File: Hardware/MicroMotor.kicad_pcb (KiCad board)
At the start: 4 copper layers, 108.4 x 72.2 mm, 109 parts, among them J1 USB_C_Receptacle_USB2.0, J2 Conn_01x04_Male, J3 Conn_01x05_Male, Q1 FDB075N15A, Q2 FDB075N15A, Q3 FDB075N15A, Q4 FDB075N15A, Q5 FDB075N15A, Q6 FDB075N15A, SW1 SW_Push, U1 FT230XQ-T, U10 LP2985-3.3, U11 NC7WZ04, U2 STM32F410RBTx, U3 ACSL-6210-00RE, U4 LM2594HVM-12, U5 INA240A3D, U6 INA240A3D, U7 LP2985-5.0, U9 HIP4086ABZ

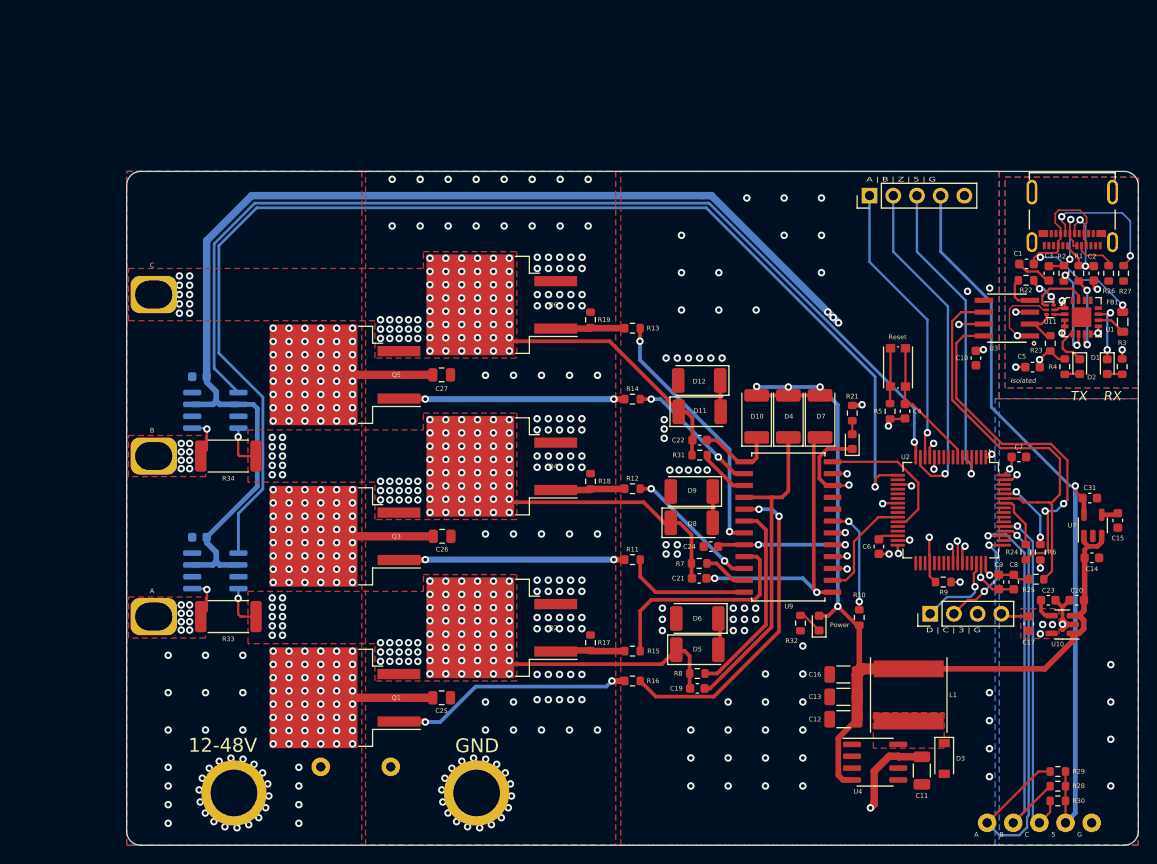
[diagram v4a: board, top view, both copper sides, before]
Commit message: Made board into pluggable two-board solution.
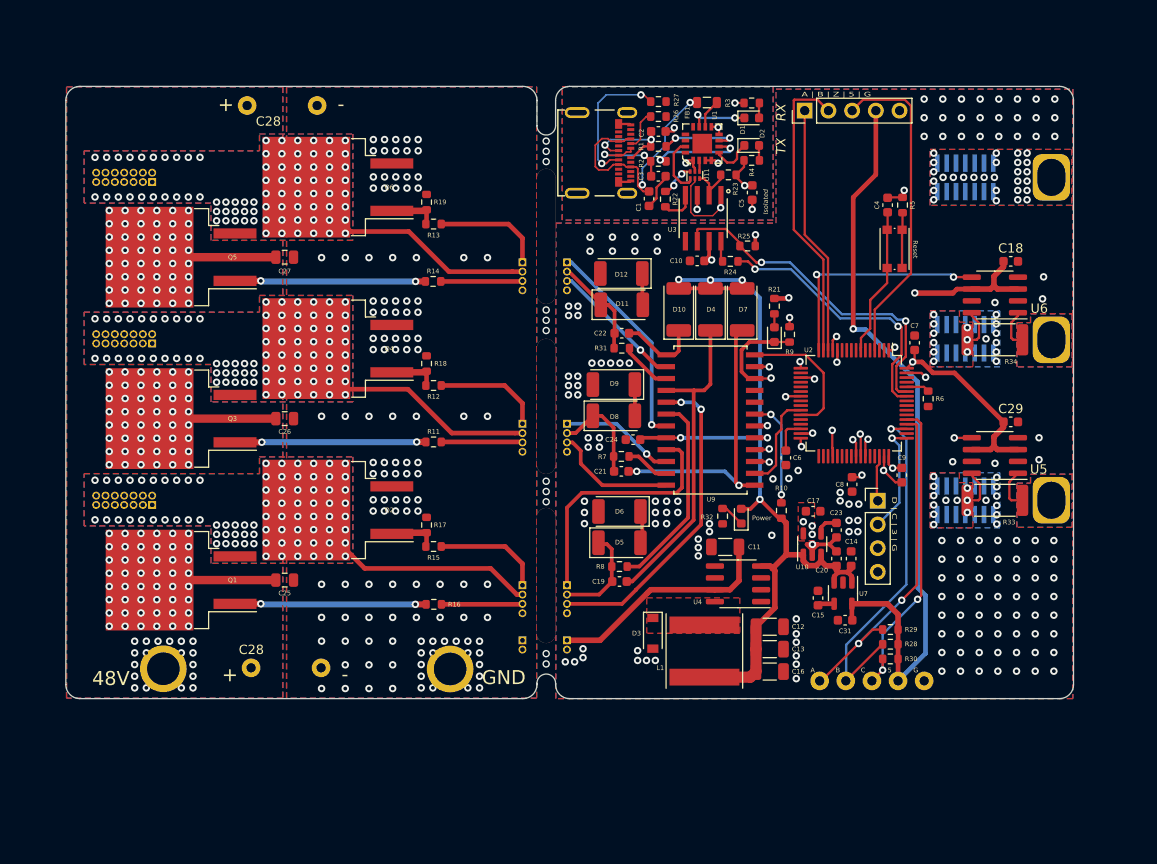
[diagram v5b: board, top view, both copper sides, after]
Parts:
- removed 12-48V: TestPoint_THTPad_D4.0mm_Drill2.0mm, TestPoint:TestPoint_THTPad_D4.0mm_Drill2.0mm
- removed the C28 at (124.0, 135.6)
- added 48V: TestPoint_THTPad_D4.0mm_Drill2.0mm, TestPoint:TestPoint_THTPad_D4.0mm_Drill2.0mm, F.Cu at (102.7, 126.1)
- added C28: 1000uF, Capacitor_THT:C_Radial_D18.0mm_H35.5mm_P7.50mm, F.Cu at (116.1, 64.7)
- added C28: 1000uF, Capacitor_THT:C_Radial_D18.0mm_H35.5mm_P7.50mm, F.Cu at (116.5, 125.0)
- added J10: Conn_02x06_Odd_Even, Connector_PinSocket_1.00mm:PinSocket_2x07_P1.00mm_Vertical_SMD, B.Cu at (193.1, 72.4)
- added J11: Conn_02x06_Odd_Even, Connector_PinSocket_1.00mm:PinSocket_2x07_P1.00mm_Vertical_SMD, B.Cu at (193.1, 89.7)
- added J12: Conn_02x06_Odd_Even, Connector_PinSocket_1.00mm:PinSocket_2x07_P1.00mm_Vertical_SMD, B.Cu at (193.1, 107.0)
- added J13: Conn_01x04_Female, Connector_PinSocket_1.00mm:PinSocket_1x04_P1.00mm_Vertical, B.Cu at (150.4, 81.5)
- added J14: Conn_01x04_Female, Connector_PinSocket_1.00mm:PinSocket_1x04_P1.00mm_Vertical, B.Cu at (150.4, 98.8)
- added J15: Conn_01x04_Female, Connector_PinSocket_1.00mm:PinSocket_1x04_P1.00mm_Vertical, B.Cu at (150.4, 116.1)
- added J16: Conn_01x02_Male, Connector_PinHeader_1.00mm:PinHeader_1x02_P1.00mm_Vertical, B.Cu at (145.6, 122.0)
- added J17: Conn_01x02_Female, Connector_PinSocket_1.00mm:PinSocket_1x02_P1.00mm_Vertical, B.Cu at (150.4, 122.0)
- added J4: Conn_01x04_Male, Connector_PinHeader_1.00mm:PinHeader_1x04_P1.00mm_Vertical, B.Cu at (145.6, 81.5)
- added J5: Conn_01x04_Male, Connector_PinHeader_1.00mm:PinHeader_1x04_P1.00mm_Vertical, B.Cu at (145.6, 98.8)
- added J6: Conn_01x04_Male, Connector_PinHeader_1.00mm:PinHeader_1x04_P1.00mm_Vertical, B.Cu at (145.6, 116.1)
- added J7: Conn_02x06_Odd_Even, Connector_PinHeader_1.00mm:PinHeader_2x07_P1.00mm_Vertical, B.Cu at (105.9, 72.9)
- added J8: Conn_02x06_Odd_Even, Connector_PinHeader_1.00mm:PinHeader_2x07_P1.00mm_Vertical, B.Cu at (105.9, 90.2)
- added J9: Conn_02x06_Odd_Even, Connector_PinHeader_1.00mm:PinHeader_2x07_P1.00mm_Vertical, B.Cu at (105.9, 107.5)
- added REF**: Test-Point-Pin_Drill2.79mm, digikey-footprints:Test-Point-Pin_Drill2.79mm, F.Cu at (148.2, 115.1)
- added REF**: Test-Point-Pin_Drill2.79mm, digikey-footprints:Test-Point-Pin_Drill2.79mm, F.Cu at (148.2, 97.0)
- added REF**: Test-Point-Pin_Drill2.79mm, digikey-footprints:Test-Point-Pin_Drill2.79mm, F.Cu at (148.2, 78.8)
- A, B, C: moved to B.Cu
- C18, C29, U5, U6: moved to F.Cu
- moved C 97.6 mm to (202.7, 72.3), turned to 270 degrees
- moved A 97.6 mm to (202.7, 106.9), turned to 270 degrees
- moved B 97.6 mm to (202.7, 89.7), turned to 270 degrees
- moved C18 87.8 mm to (197.9, 81.4), turned to 180 degrees
- moved C29 87.8 mm to (197.9, 98.6), turned to 180 degrees
- moved U5 84.4 mm to (196.2, 102.2), turned to 180 degrees
- moved U6 84.4 mm to (196.2, 85.0), turned to 180 degrees
- moved R33 83.1 mm to (196.2, 107.0), turned to 180 degrees
- moved R34 83.1 mm to (196.2, 89.8), turned to 180 degrees
- moved R27 53.1 mm to (160.2, 64.3), turned to 0 degrees
- moved J1 51.4 mm to (153.5, 69.8), turned to 270 degrees
- moved R26 51.1 mm to (160.2, 65.9), turned to 0 degrees
- moved FB1 50.4 mm to (165.4, 64.4), turned to 180 degrees
- moved C2 49.1 mm to (160.2, 67.5), turned to 0 degrees
- moved R3 48.7 mm to (170.2, 64.5), turned to 0 degrees
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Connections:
- net Net-(R11-Pad1) renamed BHO_r
- net Net-(R12-Pad1) renamed BLO_r
- net Net-(R13-Pad1) renamed CLO_r
- net Net-(R14-Pad1) renamed CHO_r
- net Net-(R15-Pad1) renamed ALO_r
- net Net-(R16-Pad1) renamed AHO_r
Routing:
- net A_SENS: track 130.7 -> 22.5 mm, vias 1 -> 2
- net +3V3: track 143.5 -> 53.0 mm, vias 16 -> 15
- net B_SENS: track 108.2 -> 25.0 mm, vias 1 -> 2
- net Net-(R24-Pad1): track 38.1 -> 2.23 mm, vias 2 -> 0
- net USART1_TX: track 5.90 -> 29.5 mm, vias 0 -> 2
- net 12V_Out: track 117.8 -> 97.1 mm
- net +48V: track 113.6 -> 97.7 mm, vias 180 -> 162
- net ALO_r: track 23.4 -> 38.9 mm
- net HALL_A: track 47.7 -> 36.1 mm, vias 1 -> 2
- net BLO_r: track 14.5 -> 24.0 mm, vias 2 -> 1
- net CHO_r: track 14.4 -> 23.2 mm, vias 2 -> 1
- net USART1_RX: track 45.4 -> 36.8 mm, vias 0 -> 2
- net BHO_r: track 13.7 -> 22.1 mm
- net AHO_r: track 34.9 -> 43.0 mm
- net CLO_r: track 27.4 -> 35.0 mm, vias 2 -> 1
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- added copper zone on B.Cu, net +48V
- added copper zone on B.Cu, net A_OUT
- added copper zone on B.Cu, net B_OUT
- added copper zone on B.Cu, net MTR_A
- added copper zone on B.Cu, net MTR_B
- added copper zone on B.Cu, net MTR_C
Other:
- board size 108.4 x 72.2 mm -> 108 x 65.6 mm
- board text added: "+"
- board text added: "-"

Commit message: More board finalization. More low ESR caps on power stage. Silkscreen fixes.
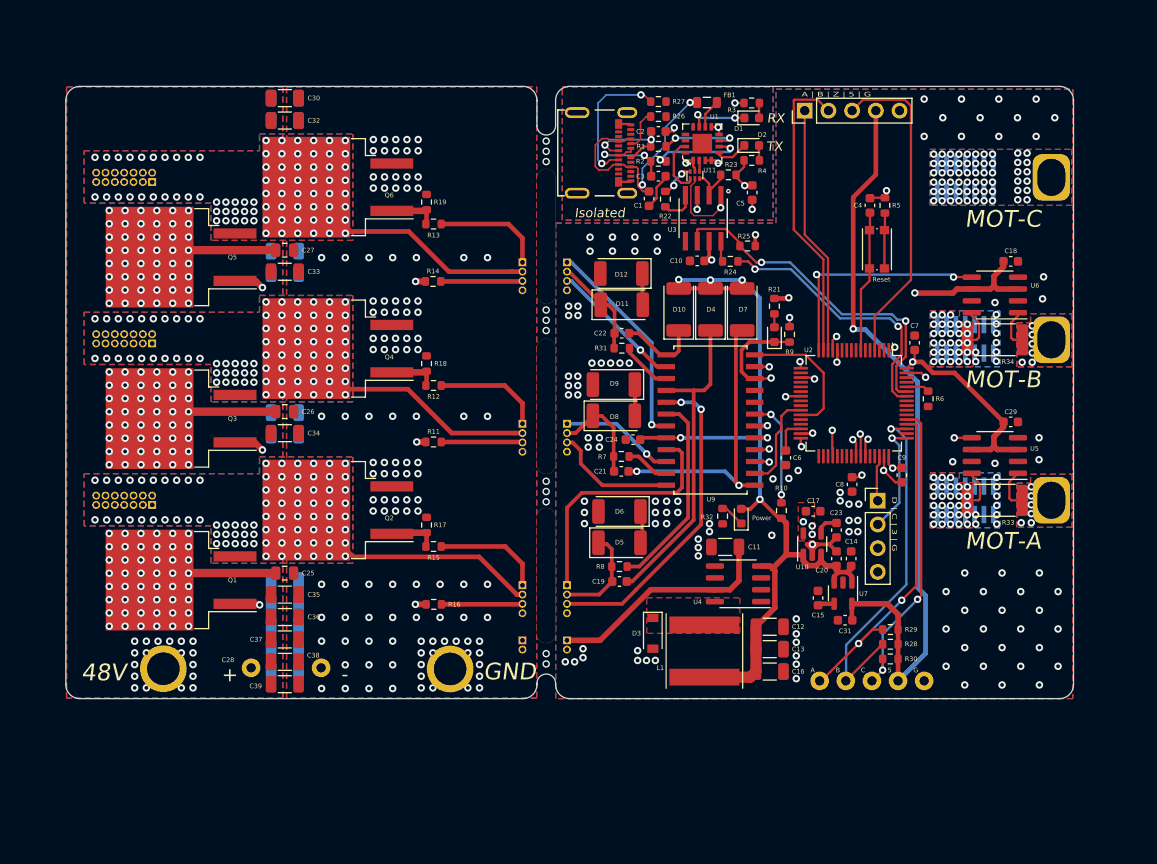
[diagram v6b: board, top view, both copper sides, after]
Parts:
- removed the C28 at (116.1, 64.7)
- added C30: 4.7uF, Capacitor_SMD:C_1206_3216Metric, F.Cu at (120.2, 64.0)
- added C32: 4.7uF, Capacitor_SMD:C_1206_3216Metric, F.Cu at (120.2, 66.3)
- added C33: 4.7uF, Capacitor_SMD:C_1206_3216Metric, F.Cu at (120.2, 82.5)
- added C34: 4.7uF, Capacitor_SMD:C_1206_3216Metric, F.Cu at (120.2, 99.8)
- added C35: 4.7uF, Capacitor_SMD:C_1206_3216Metric, F.Cu at (120.2, 117.2)
- added C36: 4.7uF, Capacitor_SMD:C_1206_3216Metric, F.Cu at (120.2, 119.5)
- added C37: 4.7uF, Capacitor_SMD:C_1206_3216Metric, F.Cu at (120.2, 122.0)
- added C38: 4.7uF, Capacitor_SMD:C_1206_3216Metric, F.Cu at (120.2, 124.3)
- added C39: 4.7uF, Capacitor_SMD:C_1206_3216Metric, F.Cu at (120.2, 126.8)
- added C40: 4.7uF, Capacitor_SMD:C_1206_3216Metric, B.Cu at (120.2, 64.0)
- added C41: 4.7uF, Capacitor_SMD:C_1206_3216Metric, B.Cu at (120.2, 66.3)
- added C42: 4.7uF, Capacitor_SMD:C_1206_3216Metric, B.Cu at (120.2, 80.3)
- added C43: 4.7uF, Capacitor_SMD:C_1206_3216Metric, B.Cu at (120.2, 82.8)
- added C44: 4.7uF, Capacitor_SMD:C_1206_3216Metric, B.Cu at (120.2, 97.7)
- added C45: 4.7uF, Capacitor_SMD:C_1206_3216Metric, B.Cu at (120.2, 100.0)
- added C46: 4.7uF, Capacitor_SMD:C_1206_3216Metric, B.Cu at (120.2, 115.7)
- added C47: 4.7uF, Capacitor_SMD:C_1206_3216Metric, B.Cu at (120.2, 118.0)
- added C48: 4.7uF, Capacitor_SMD:C_1206_3216Metric, B.Cu at (120.2, 120.5)
- added C49: 4.7uF, Capacitor_SMD:C_1206_3216Metric, B.Cu at (120.2, 122.8)
- added C50: 4.7uF, Capacitor_SMD:C_1206_3216Metric, B.Cu at (120.2, 125.2)
- added G***: LOGO, kyleRhess_logos:umotor1_silk, B.Cu at (165.8, 116.5)
- added G***: LOGO, kyleRhess_logos:umotor1, F.Cu at (108.2, 66.2)
- added G***: LOGO, kyleRhess_logos:kylerhess_github, B.Cu at (136.1, 64.9)
- added G***: LOGO, kyleRhess_logos:rev_0p2, B.Cu at (158.0, 118.5)
- added REF**: KiCad-Logo2_6mm_SilkScreen, Symbol:KiCad-Logo2_6mm_SilkScreen, B.Cu at (196.3, 122.5)
- moved C4 1.89 mm to (182.8, 75.4)
- moved R5 1.89 mm to (184.4, 75.4)
- moved SW1 1.89 mm to (183.6, 80.1)
- moved C25 0.75 mm to (120.1, 114.8)
- moved C26 0.75 mm to (120.1, 97.5)
- moved C27 0.75 mm to (120.1, 80.2)
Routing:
- net Net-(D2-Pad1): track 4.41 -> 3.55 mm
- net Net-(C4-Pad1): track 16.0 -> 15.2 mm
- net BHO: track 20.5 -> 21.1 mm
- net CHO: track 20.4 -> 21.0 mm
- net GND: vias 282 -> 238
- net MTR_A: vias 101 -> 119
- net MTR_C: vias 111 -> 143
- net MTR_B: vias 99 -> 119
- net B_OUT: vias 0 -> 6
- net A_OUT: vias 0 -> 6
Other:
- board text added: "MOT-A"
- board text added: "MOT-B"
- board text added: "MOT-C"

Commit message: More board refinements
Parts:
- added G***: LOGO, kyleRhess_logos:rev_0p2_cu, F.Cu at (142.8, 67.3)
- added REF**: MountingHole_2.7mm_M2.5, MountingHole:MountingHole_2.7mm_M2.5, F.Cu at (95.4, 107.1)
- added REF**: MountingHole_2.7mm_M2.5, MountingHole:MountingHole_2.7mm_M2.5, F.Cu at (95.4, 72.1)
- added REF**: MountingHole_2.7mm_M2.5, MountingHole:MountingHole_2.7mm_M2.5, F.Cu at (142.2, 107.1)
- added REF**: MountingHole_2.7mm_M2.5, MountingHole:MountingHole_2.7mm_M2.5, F.Cu at (142.2, 72.1)
- moved G*** 28.0 mm to (136.2, 65.3)
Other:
- board size 108 x 65.6 mm -> 113 x 65.6 mm
- board text added: "MOTOR-A"
- board text added: "MOTOR-B"
- board text added: "MOTOR-C"
- board text removed: "MOT-A"
- board text removed: "MOT-B"
- board text removed: "MOT-C"

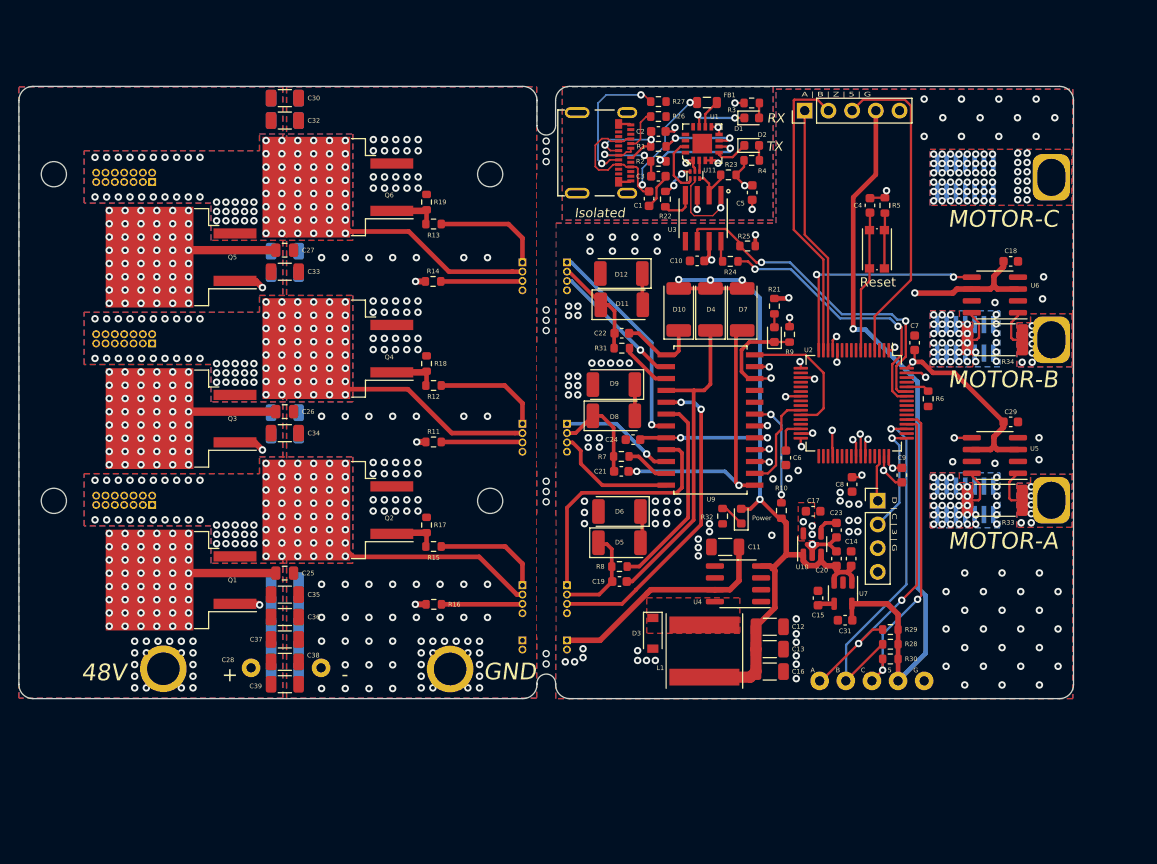
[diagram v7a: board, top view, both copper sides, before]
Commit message: Changed board connectors to 1.27mm pitch. Nearly done.
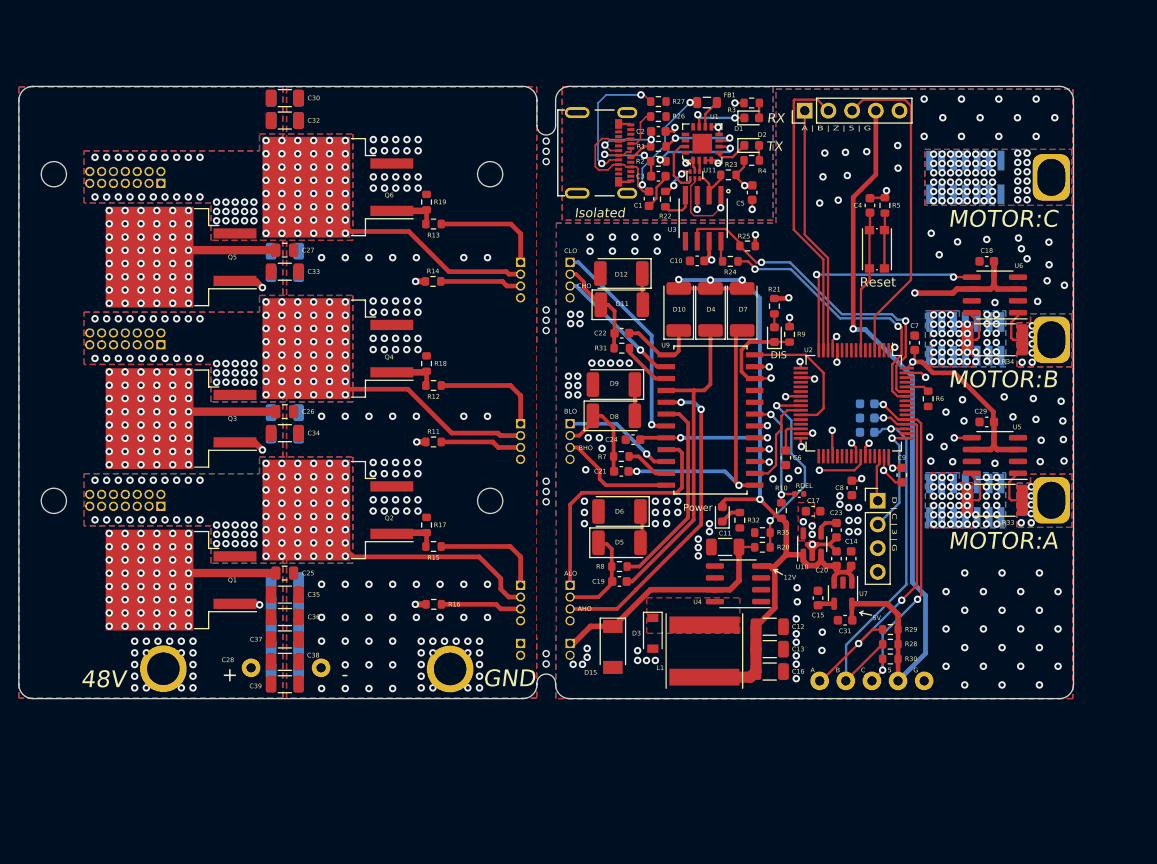
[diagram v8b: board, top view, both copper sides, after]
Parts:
- added D15: SMA6S56A, Diode_SMD:D_SOD-128, F.Cu at (155.3, 122.8)
- added R20: 10k, Resistor_SMD:R_0603_1608Metric, F.Cu at (171.3, 112.1)
- added R35: 576, Resistor_SMD:R_0603_1608Metric, F.Cu at (171.3, 110.5)
- added RDEL: C_0402_1005Metric, Capacitor_SMD:C_0402_1005Metric, F.Cu at (175.3, 106.4)
- added REF**: C_0603_1608Metric, Capacitor_SMD:C_0603_1608Metric, B.Cu at (182.6, 96.7)
- added REF**: C_0603_1608Metric, Capacitor_SMD:C_0603_1608Metric, B.Cu at (182.6, 98.2)
- added REF**: C_0603_1608Metric, Capacitor_SMD:C_0603_1608Metric, B.Cu at (182.6, 99.8)
- J10, J11, J12: footprint Connector_PinSocket_1.00mm:PinSocket_2x07_P1.00mm_Vertical_SMD -> Connector_PinSocket_1.27mm:PinSocket_2x07_P1.27mm_Vertical_SMD
- J13, J14, J15: footprint Connector_PinSocket_1.00mm:PinSocket_1x04_P1.00mm_Vertical -> Connector_PinSocket_1.27mm:PinSocket_1x04_P1.27mm_Vertical
- J16: footprint Connector_PinHeader_1.00mm:PinHeader_1x02_P1.00mm_Vertical -> Connector_PinHeader_1.27mm:PinHeader_1x02_P1.27mm_Vertical
- J17: footprint Connector_PinSocket_1.00mm:PinSocket_1x02_P1.00mm_Vertical -> Connector_PinSocket_1.27mm:PinSocket_1x02_P1.27mm_Vertical
- J4, J5, J6: footprint Connector_PinHeader_1.00mm:PinHeader_1x04_P1.00mm_Vertical -> Connector_PinHeader_1.27mm:PinHeader_1x04_P1.27mm_Vertical
- J7, J8, J9: footprint Connector_PinHeader_1.00mm:PinHeader_2x07_P1.00mm_Vertical -> Connector_PinHeader_1.27mm:PinHeader_2x07_P1.27mm_Vertical
- moved C29 2.57 mm to (195.4, 98.7), turned to 0 degrees
- moved C18 2.57 mm to (195.4, 81.4), turned to 0 degrees
- moved D13 2.04 mm to (167.0, 108.5)
- moved R32 1.90 mm to (168.9, 109.2)
- moved J7 0.95 mm to (106.9, 73.1)
- moved J8 0.95 mm to (106.9, 90.4)
- moved J9 0.95 mm to (106.9, 107.7)
- moved J17 0.47 mm to (150.7, 122.4)
- moved J16 0.39 mm to (145.4, 122.4)
- moved C8 0.38 mm to (180.9, 105.7)
- moved J13 0.33 mm to (150.7, 81.5)
- moved J14 0.33 mm to (150.7, 98.8)
- moved J15 0.33 mm to (150.7, 116.1)
- moved J4 0.20 mm to (145.4, 81.5)
- moved J5 0.20 mm to (145.4, 98.8)
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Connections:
- net Net-(R10-Pad2) renamed RDEL
- U2 pad 25: Net-(U2-Pad25) -> VBAT_MEAS
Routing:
- net VBAT_MEAS: track 0.00 -> 20.6 mm, vias 0 -> 2
- net HALL_C: track 32.7 -> 36.8 mm, vias 2 -> 3
- net HALL_A: track 36.1 -> 39.9 mm, vias 2 -> 3
- net BLI: track 15.5 -> 12.9 mm
- net 12V_Out: track 97.1 -> 99.3 mm
- net +48V: track 97.7 -> 99.8 mm
- net HALL_B: track 38.1 -> 40.0 mm
- net RDEL: track 11.7 -> 13.2 mm
- net +3V3: track 53.0 -> 51.8 mm
- net BHO_r: track 22.1 -> 21.3 mm
- net ALI: track 13.3 -> 12.7 mm
- net CHO_r: track 23.2 -> 22.6 mm
- net MTR_A: track 41.8 -> 42.3 mm, vias 119 -> 125
- net MTR_B: track 42.2 -> 42.3 mm, vias 119 -> 125
- net GND: vias 238 -> 274
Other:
- board text added: "12V"
- board text added: "5V"
- board text added: "AHO"
- board text added: "ALO"
- board text added: "BHO"
- board text added: "BLO"
- board text added: "CHO"
- board text added: "CLO"
- board text added: "DIS"
- board text added: "MOTOR:A"
- board text added: "MOTOR:B"
- board text added: "MOTOR:C"
- board text removed: "MOTOR-A"
- board text removed: "MOTOR-B"
- board text removed: "MOTOR-C"
